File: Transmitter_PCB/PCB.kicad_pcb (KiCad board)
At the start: 2 copper layers, 130.8 x 85.1 mm, 51 parts, among them J1 Conn_01x04_Female, J10 Conn_01x08_Female, J11 Conn_01x01_Female, J12 Conn_01x04_Female, J13 Conn_01x02_Female, J2 Conn_01x28_Female, J3 Conn_01x02_Female, J4 Conn_01x02_Female, J5 Conn_01x02_Female, J6 Conn_01x02_Female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

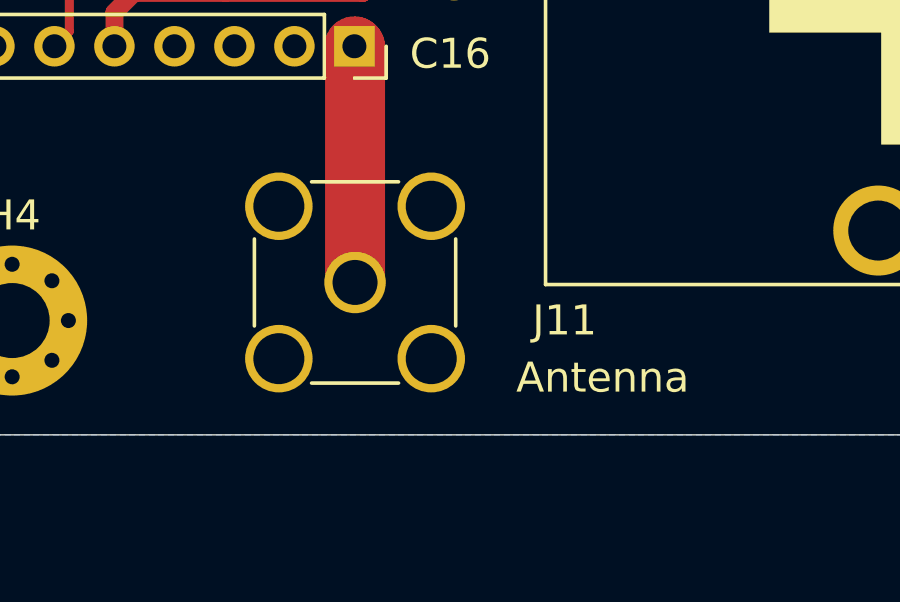
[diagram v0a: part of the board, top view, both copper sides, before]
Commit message: Changed RFM95W footprint and added SMA Connector Model
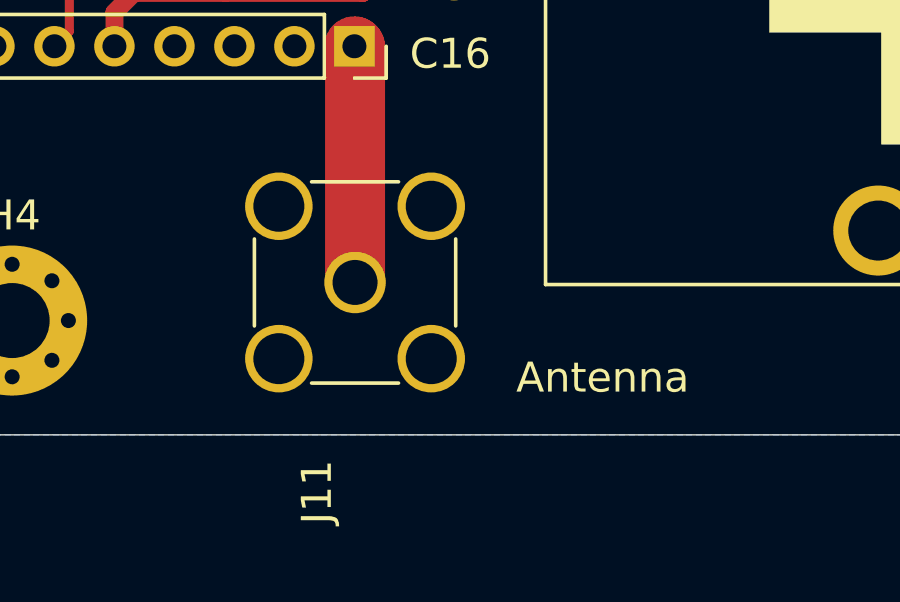
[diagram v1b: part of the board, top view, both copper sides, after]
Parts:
- turned J11 to 270 degrees
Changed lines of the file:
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@@
   )
   (module Connector_Coaxial:SMA_Amphenol_901-144_Vertical (layer F.Cu)
-    (at 147.32 97.79)
+    (at 147.32 97.79 270)
     (descr https://www.amphenolrf.com/downloads/dl/file/id/7023/product/3103/901_144_customer_drawing.pdf)
     (tags "SMA THT Female Jack Vertical")
-    (fp_text reference J11 (at 6.985 1.27) (layer F.SilkS)
-      (effects (font (size 1 1) (thickness 0.15)))
-    )
-    (fp_text value Conn_01x01_Female (at 12.7 2.54) (layer F.Fab)
+    (fp_text reference J11 (at 6.985 1.27 270) (layer F.SilkS)
+      (effects (font (size 1 1) (thickness 0.15)))
+    )
+    (fp_text value Conn_01x01_Female (at 12.7 2.54 270) (layer F.Fab)
       (effects (font (size 1 1) (thickness 0.15)))
     )
@@
     (fp_line (start -1.45 3.355) (end 1.45 3.355) (layer F.SilkS) (width 0.12))
     (fp_line (start -1.45 -3.355) (end 1.45 -3.355) (layer F.SilkS) (width 0.12))
-    (fp_text user %R (at 0 0) (layer F.Fab)
-      (effects (font (size 1 1) (thickness 0.15)))
-    )
-    (pad 1 thru_hole circle (at 0 0) (size 2.05 2.05) (drill 1.5) (layers *.Cu *.Mask)
+    (fp_text user %R (at 0 0 270) (layer F.Fab)
+      (effects (font (size 1 1) (thickness 0.15)))
+    )
+    (pad 1 thru_hole circle (at 0 0 270) (size 2.05 2.05) (drill 1.5) (layers *.Cu *.Mask)
       (net 28 ANT))
-    (pad 2 thru_hole circle (at 2.54 2.54) (size 2.25 2.25) (drill 1.7) (layers *.Cu *.Mask))
-    (pad 2 thru_hole circle (at 2.54 -2.54) (size 2.25 2.25) (drill 1.7) (layers *.Cu *.Mask))
-    (pad 2 thru_hole circle (at -2.54 -2.54) (size 2.25 2.25) (drill 1.7) (layers *.Cu *.Mask))
-    (pad 2 thru_hole circle (at -2.54 2.54) (size 2.25 2.25) (drill 1.7) (layers *.Cu *.Mask))
+    (pad 2 thru_hole circle (at 2.54 2.54 270) (size 2.25 2.25) (drill 1.7) (layers *.Cu *.Mask))
+    (pad 2 thru_hole circle (at 2.54 -2.54 270) (size 2.25 2.25) (drill 1.7) (layers *.Cu *.Mask))
+    (pad 2 thru_hole circle (at -2.54 -2.54 270) (size 2.25 2.25) (drill 1.7) (layers *.Cu *.Mask))
+    (pad 2 thru_hole circle (at -2.54 2.54 270) (size 2.25 2.25) (drill 1.7) (layers *.Cu *.Mask))
     (model ${KISYS3DMOD}/Connector_Coaxial.3dshapes/SMA_Amphenol_901-144_Vertical.wrl
       (at (xyz 0 0 0))
       (scale (xyz 1 1 1))
       (rotate (xyz 0 0 0))
+    )
+    (model "C:/Users/Toni/Desktop/Free Public Bicycles/Gateway_PCB/132203_3d_model_file.STEP"
+      (offset (xyz 2.25 -0.5 6.5))
+      (scale (xyz 1 1 1))
+      (rotate (xyz 85 0 0))
     )
   )
@@
   (gr_line (start 48.26 102.87) (end 166.37 102.87) (layer Edge.Cuts) (width 0.05))
   (gr_line (start 46.99 96.52) (end 46.99 19.05) (layer Edge.Cuts) (width 0.05))
-  (segment (start 95.885 24.13) (end 95.885 26.67) (width 1.27) (layer F.Cu) (net 41))
-  (segment (start 95.885 26.67) (end 97.155 26.67) (width 1.27) (layer F.Cu) (net 41))
-  (segment (start 99.695 26.67) (end 100.965 26.67) (width 1.27) (layer F.Cu) (net 41))
-  (segment (start 100.965 26.67) (end 107.315 26.67) (width 1.27) (layer F.Cu) (net 41))
-  (segment (start 99.695 26.67) (end 97.155 26.67) (width 1.27) (layer F.Cu) (net 41))
-  (segment (start 113.03 26.67) (end 107.315 26.67) (width 1.27) (layer F.Cu) (net 41))
-  (segment (start 125.095 26.67) (end 113.03 26.67) (width 1.27) (layer F.Cu) (net 41))
-  (segment (start 130.175 31.75) (end 125.095 26.67) (width 1.27) (layer F.Cu) (net 41))
-  (segment (start 157.48 31.75) (end 130.175 31.75) (width 1.27) (layer F.Cu) (net 41))
-  (segment (start 164.76 24.66) (end 164.57 24.66) (width 1.27) (layer F.Cu) (net 41))
-  (segment (start 164.57 24.66) (end 157.48 31.75) (width 1.27) (layer F.Cu) (net 41))
   (segment (start 58.42 64.77) (end 64.77 64.77) (width 1.27) (layer F.Cu) (net 1))
   (segment (start 116.84 81.28) (end 114.844999 79.284999) (width 0.6) (layer F.Cu) (net 2))
@@
   (segment (start 109.22 66.04) (end 110.32 66.04) (width 0.3) (layer F.Cu) (net 40))
   (segment (start 110.32 66.04) (end 111.59 64.77) (width 0.3) (layer F.Cu) (net 40))
+  (segment (start 95.885 24.13) (end 95.885 26.67) (width 1.27) (layer F.Cu) (net 41))
+  (segment (start 95.885 26.67) (end 97.155 26.67) (width 1.27) (layer F.Cu) (net 41))
+  (segment (start 99.695 26.67) (end 100.965 26.67) (width 1.27) (layer F.Cu) (net 41))
+  (segment (start 100.965 26.67) (end 107.315 26.67) (width 1.27) (layer F.Cu) (net 41))
+  (segment (start 99.695 26.67) (end 97.155 26.67) (width 1.27) (layer F.Cu) (net 41))
+  (segment (start 113.03 26.67) (end 107.315 26.67) (width 1.27) (layer F.Cu) (net 41))
+  (segment (start 125.095 26.67) (end 113.03 26.67) (width 1.27) (layer F.Cu) (net 41))
+  (segment (start 130.175 31.75) (end 125.095 26.67) (width 1.27) (layer F.Cu) (net 41))
+  (segment (start 157.48 31.75) (end 130.175 31.75) (width 1.27) (layer F.Cu) (net 41))
+  (segment (start 164.76 24.66) (end 164.57 24.66) (width 1.27) (layer F.Cu) (net 41))
+  (segment (start 164.57 24.66) (end 157.48 31.75) (width 1.27) (layer F.Cu) (net 41))
   (segment (start 164.76 49.87) (end 164.76 24.66) (width 0.6) (layer F.Cu) (net 41) (status 1000000))
   (segment (start 149.86 64.77) (end 164.76 49.87) (width 0.6) (layer F.Cu) (net 41) (status 1000000))

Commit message: Fixed LoRa socket
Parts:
- J13: value Conn_01x02_Female -> Conn_01x03_Female; footprint Connector_PinSocket_2.54mm:PinSocket_1x02_P2.54mm_Vertical -> Connector_PinSocket_2.54mm:PinSocket_1x03_P2.54mm_Vertical
- moved J13 16.8 mm to (105.2, 61.0)
- moved J11 14.0 mm to (133.3, 98.3)
- moved H3 11.2 mm to (147.1, 22.1)
- moved H4 11.2 mm to (147.1, 99.1)
- moved C16 5.14 mm to (151.4, 90.2), turned to 90 degrees
- moved C2 1.78 mm to (102.4, 72.9)
- moved C5 1.27 mm to (120.7, 78.7)
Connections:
- J10 pad 1: ANT -> Net-(J10-Pad1)
- J10 pad 2: GND -> Net-(J10-Pad2)
- J10 pad 3: Net-(J10-Pad3) -> DIO0
- J10 pad 4: Net-(J10-Pad4) -> +3V3
- J10 pad 5: +3V3 -> Net-(J10-Pad5)
- J10 pad 6: DIO0 -> Net-(J10-Pad6)
- J10 pad 7: Net-(J10-Pad7) -> GND
- J10 pad 8: Net-(J10-Pad8) -> ANT
- J13 pad 1: UART_RX -> RESET
- J13 pad 2: UART_TX -> UART_RX
- J2 pad 1: Net-(J2-Pad1) -> RESET
- R1 pad 2: Net-(J2-Pad1) -> RESET
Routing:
- net UART_TX: track 14.1 -> 4.06 mm
- net RESET: track 40.2 -> 50.1 mm
- net UART_RX: track 13.2 -> 4.06 mm
- net DIO0: track 71.1 -> 64.1 mm
- net Net-(J2-Pad1): track 5.87 -> 0.00 mm
- net +3V3: track 50.3 -> 53.2 mm
- net +5V: track 107.1 -> 109.4 mm
- net Net-(C5-Pad1): track 4.34 -> 3.81 mm
- net ANT: track 7.88 -> 8.40 mm
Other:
- board text added: "+"
- board text added: "-"
- board text removed: "RX"
- board text removed: "TX"

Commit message: Fixed Transmitter PCB Spacing
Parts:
- J13: value Conn_01x03_Female -> Conn_01x04_Female; footprint Connector_PinSocket_2.54mm:PinSocket_1x03_P2.54mm_Vertical -> Connector_PinSocket_2.54mm:PinSocket_1x04_P2.54mm_Vertical
- J8: footprint Connector_Molex:Molex_PicoBlade_53047-0210_1x02_P1.25mm_Vertical -> Connector_Molex:Molex_KK-254_AE-6410-02A_1x02_P2.54mm_Vertical
- moved J6 13.7 mm to (95.6, 21.8)
- moved J4 13.7 mm to (76.6, 24.4)
- moved J5 9.15 mm to (95.6, 33.3)
- moved J3 9.15 mm to (76.6, 35.8)
- moved C7 7.62 mm to (61.3, 31.8)
- moved C8 7.62 mm to (69.0, 31.8)
- moved C19 6.29 mm to (90.8, 41.9)
- moved J12 4.83 mm to (83.8, 46.0)
- moved C6 1.27 mm to (54.6, 44.5)
- moved C11 1.27 mm to (102.2, 26.7)
- moved J8 0.46 mm to (101.9, 98.7)
- moved J13 0.13 mm to (105.0, 61.0)
- moved C16 0.13 mm to (151.3, 90.2)
- turned C17 to 270 degrees
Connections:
- J13 pad 1: RESET -> RST
- J2 pad 1: RESET -> RST
- R1 pad 2: RESET -> RST
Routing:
- net RST: track 0.00 -> 9.93 mm
- net RESET: track 50.1 -> 40.2 mm
- net Net-(C6-Pad1): track 82.1 -> 74.5 mm
- net RX: track 57.0 -> 61.8 mm
- net TX: track 69.7 -> 74.2 mm
- net VBAT: track 122.7 -> 127.2 mm
- net VCCGPS: track 28.0 -> 25.5 mm
- net Net-(J8-Pad1): track 6.35 -> 7.33 mm
- net Net-(J2-Pad26): track 23.9 -> 23.4 mm
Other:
- board text added: "."
- board text added: "GND"
- board text added: "Vin"
- board text added: "Vo"
- board text removed: "Antoan Yanev-2020 v1.0"

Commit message: Added 3d models
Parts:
- removed J10, J7: Conn_01x08_Female, Connector_PinSocket_2.00mm:PinSocket_1x08_P2.00mm_Vertical
- removed J3, J4, J5, J6: Conn_01x02_Female, Connector_PinSocket_2.54mm:PinSocket_1x02_P2.54mm_Vertical
- added U2: MP1584, MyComponents:MP1584, F.Cu at (95.6, 28.2)
- added U3: RFM95W-868S2, MyComponents:RFM95W_THT, F.Cu at (147.4, 76.5)
- H1, H2, H3, H4: value MountingHole_2.5mm_Pad_Via -> MountingHole; footprint MountingHole:MountingHole_2.5mm_Pad_Via -> MountingHole:MountingHole_3.5mm_Pad_Via
- moved H4 76.5 mm to (147.6, 22.6)
- moved H3 76.2 mm to (147.7, 98.3)
- moved C13 4.45 mm to (118.7, 26.7)
- moved C19 4.45 mm to (86.4, 41.9), turned to 180 degrees
- moved C14 4.44 mm to (125.1, 26.7)
- moved C7 2.79 mm to (64.1, 31.8), turned to 90 degrees
- moved C11 2.54 mm to (99.7, 26.7), turned to 90 degrees
- moved C8 2.16 mm to (71.1, 31.8), turned to 90 degrees
- moved H2 1.27 mm to (51.6, 22.6)
- moved C12 1.27 mm to (106.0, 26.7), turned to 90 degrees
- moved H1 1.08 mm to (51.6, 98.3)
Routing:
- net Net-(C6-Pad1): track 74.5 -> 71.9 mm

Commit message: Added Gerber Files
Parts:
- moved C16 17.3 mm to (150.9, 72.9), turned to 180 degrees
- moved J11 14.2 mm to (147.6, 97.8)
- moved U3 13.1 mm to (134.4, 76.5), turned to 0 degrees
- moved H4 11.7 mm to (135.9, 22.9)
- moved H3 11.6 mm to (136.1, 98.0)
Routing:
- net BUTTON: track 89.4 -> 66.2 mm
- net MISO: track 41.7 -> 20.3 mm
- net MOSI: track 40.3 -> 20.6 mm
- net DIO0: track 64.1 -> 44.4 mm
- net +3V3: track 53.0 -> 33.4 mm
- net SCK: track 47.3 -> 29.0 mm
- net NSS: track 36.8 -> 19.9 mm
- net RESET: track 40.2 -> 29.9 mm
- net ANT: track 8.40 -> 7.27 mm
